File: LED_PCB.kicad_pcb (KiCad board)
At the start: 4 copper layers, 39.8 x 39.8 mm, 178 parts, among them J1 +5v Pad, J10 UART Debug, J11 UART Top (RX), J12 UART Bottom (TX), J13 UART Left (RX), J14 UART Right (TX), J15 ENA Pad, J16 MTX Out Conn, J2 +5v Pad, J3 +5v Pad, J4 +5v Pad, J5 GND Pad, J6 GND Pad, J7 GND Pad, J8 GND Pad, J9 ST-Link Conn, P1 USB_C_Plug_USB2.0, Q1 Si2319CDS, Q2 BSS138, SW1 SW_DP3T, SW2 SW_reset, SW3 SW_DPDT_x2, U1 AMS1117-3.3, U2 TPD4EUSB30, U3 STM32F103C8Tx, Y1 8MHz

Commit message: Inited repo
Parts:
- removed P1: USB_C_Plug_USB2.0, Connector_USB:USB_C_Receptacle_Amphenol_12401610E4-2A_CircularHoles
- added C76: 4.7u, Capacitor_Tantalum_SMD:CP_EIA-3216-12_Kemet-S, F.Cu at (79.4, 52.2)
- added J17: USB_C_Receptacle_USB2.0, LED_PCB_LIB:USB_C_Connector_16P_SMD, F.Cu at (74.5, 40.0)
- added R11: 1k5, Resistor_SMD:R_0402_1005Metric, F.Cu at (95.7, 35.0)
- added R12: 5.1k, Resistor_SMD:R_0402_1005Metric, F.Cu at (77.7, 41.8)
- added R13: 5.1k, Resistor_SMD:R_0402_1005Metric, F.Cu at (77.7, 38.8)
- C1: value 22u t -> 4.7u; footprint Capacitor_SMD:C_0504_1310Metric -> Capacitor_Tantalum_SMD:CP_EIA-3216-12_Kemet-S
- C12, C13, C14, C15, C16, C17, C18, C19, C20, C21, C22, C23, C24, C25, C26, C27, C28, C29, C30, C31, C32, C33, C34, C35, C36, C37, C38, C39, C40, C41, C42, C43, C44, C45, C46, C47, C48, C49, C50, C51, C52, C53, C54, C55, C56, C57, C58, C59, C60, C61, C62, C63, C64, C65, C66, C67, C68, C69, C70, C71, C72, C73, C74, C75: moved to F.Cu
- C2: footprint Capacitor_SMD:C_0504_1310Metric -> Capacitor_SMD:C_0805_2012Metric
- C5: value 4.7u -> 22u t
- moved C68 82.5 mm to (30.9, 30.8), turned to 0 degrees
- moved C52 77.0 mm to (33.4, 29.0), turned to 0 degrees
- moved C60 73.4 mm to (40.7, 27.2), turned to 0 degrees
- moved J16 72.6 mm to (124.1, 17.9), turned to 0 degrees
- moved C36 69.9 mm to (35.8, 34.2), turned to 0 degrees
- moved C70 68.5 mm to (35.8, 29.0), turned to 0 degrees
- moved C62 67.9 mm to (30.9, 39.5), turned to 0 degrees
- moved C53 67.2 mm to (38.2, 30.8), turned to 0 degrees
- moved J10 67.1 mm to (124.1, 21.2), turned to 0 degrees
- moved C69 66.8 mm to (40.7, 32.5), turned to 0 degrees
- moved C55 64.1 mm to (30.9, 32.5), turned to 0 degrees
- moved C13 63.6 mm to (35.8, 27.2), turned to 0 degrees
- moved C20 63.3 mm to (40.7, 37.8), turned to 0 degrees
- moved C38 63.0 mm to (33.4, 32.5), turned to 0 degrees
- moved C63 63.0 mm to (38.2, 27.2), turned to 0 degrees
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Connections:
- net /USB_DM renamed /USB_D-
- net /USB_DP renamed /USB_D+
- C5 pad 1: +3V3 -> +5V
- J9 pad 2: /SWCLK -> unconnected-(J9-Pad2)
- J9 pad 3: /SWDIO -> /SWCLK
- J9 pad 4: /NRST -> /SWDIO
- J9 pad 5: (no net) -> /NRST
- Q2 pad 2: /LED_MATRIX -> Net-(Q2-Pad2)
- R5 pad 1: /HSE_OUT -> Net-(C4-Pad1)
- R5 pad 2: Net-(C4-Pad1) -> /HSE_OUT
- R9 pad 1: /LED_MATRIX -> Net-(Q2-Pad2)
- U2 pad 5: (no net) -> unconnected-(U2-Pad5)
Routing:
- net +3V3: track 7.67 -> 47.2 mm, vias 0 -> 6
- net Net-(D51-Pad1): track 39.2 -> 5.56 mm
- net Net-(D59-Pad1): track 39.2 -> 5.56 mm
- net Net-(D19-Pad1): track 39.2 -> 5.56 mm
- net Net-(D27-Pad1): track 39.2 -> 5.61 mm
- net Net-(D11-Pad1): track 39.2 -> 5.67 mm
- net Net-(D35-Pad1): track 39.2 -> 6.67 mm, vias 0 -> 2
- net Net-(D43-Pad1): track 39.2 -> 8.11 mm, vias 0 -> 2
- net /UART2_TX: track 0.00 -> 26.7 mm, vias 0 -> 1
- net GND: track 7.81 -> 29.4 mm, vias 1 -> 21
- net /ENA_PIN: track 0.00 -> 17.2 mm
- net +5V: track 4.57 -> 20.3 mm, vias 1 -> 19
- net /BOOT0: track 0.00 -> 14.6 mm
- net /USB_D+: track 0.00 -> 14.5 mm
- net /USB_D-: track 0.00 -> 13.5 mm
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- added copper zone on F.Cu, net +3V3
- added copper zone on In1.Cu, net +3V3
- added copper zone on B.Cu, net +5V
- added copper zone on F.Cu, net +5V
- added copper zone on In2.Cu, net +5V
- added copper zone on B.Cu, net GND
- added copper zone on F.Cu, net GND
- added copper zone on In2.Cu, net GND
- added copper zone on B.Cu, net Net-(J1-Pad1)
- added copper zone on F.Cu, net Net-(J1-Pad1)
- added copper zone on In1.Cu, net Net-(J1-Pad1)
- removed copper zone on In1.Cu, net +5V
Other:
- board size 39.8 x 39.8 mm -> 40.3 x 39.8 mm

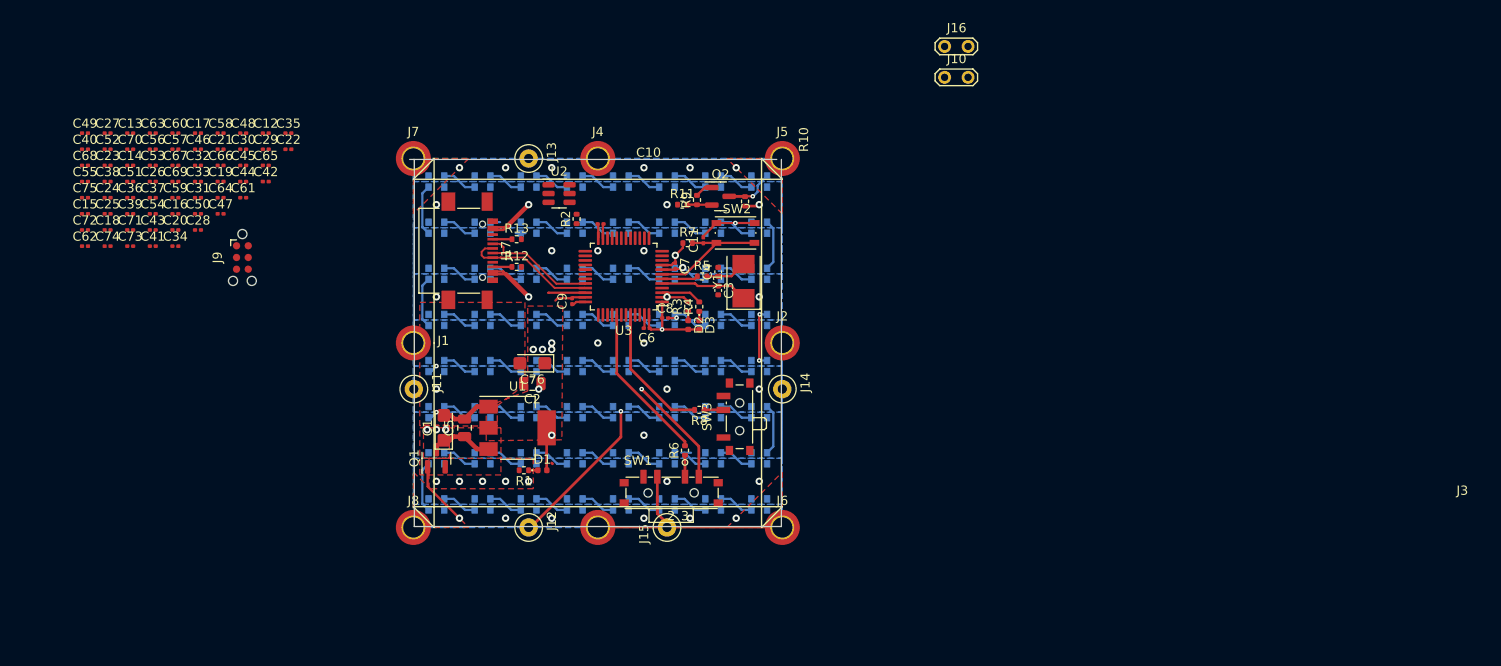
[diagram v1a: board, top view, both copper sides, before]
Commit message: traced power polygons
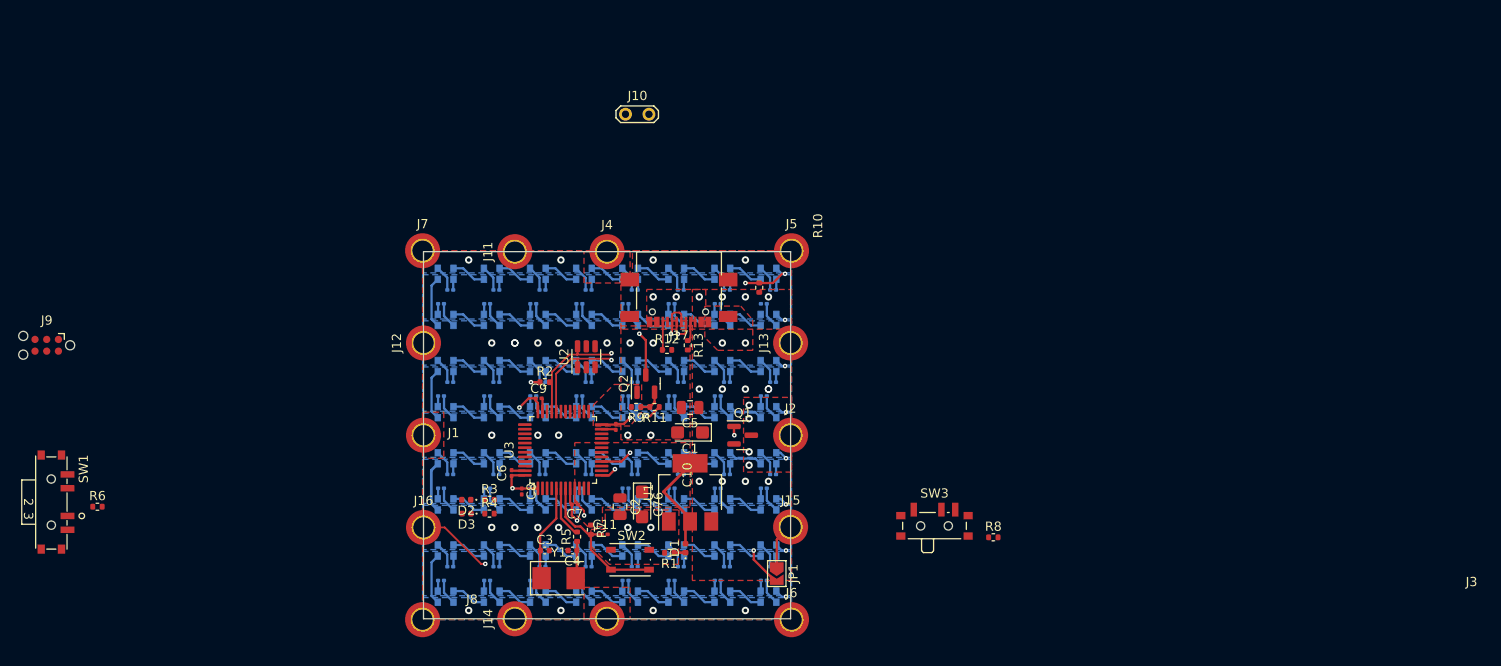
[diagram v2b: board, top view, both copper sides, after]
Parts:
- added JP1: Jumper_2_Open, Jumper:SolderJumper-2_P1.3mm_Open_TrianglePad1.0x1.5mm, F.Cu at (105.9, 75.0)
- C12, C13, C14, C15, C16, C17, C18, C19, C20, C21, C22, C23, C24, C25, C26, C27, C28, C29, C30, C31, C32, C33, C34, C35, C36, C37, C38, C39, C40, C41, C42, C43, C44, C45, C46, C47, C48, C49, C50, C51, C52, C53, C54, C55, C56, C57, C58, C59, C60, C61, C62, C63, C64, C65, C66, C67, C68, C69, C70, C71, C72, C73, C74, C75: moved to B.Cu
- J11, J12, J13, J14: footprint TestPoint:TestPoint_Loop_D1.80mm_Drill1.0mm_Beaded -> MountingHole:MountingHole_2.2mm_M2_DIN965_Pad_TopOnly
- J15: value ENA Pad -> LED_MATRIX_IN; footprint TestPoint:TestPoint_Loop_D1.80mm_Drill1.0mm_Beaded -> MountingHole:MountingHole_2.2mm_M2_DIN965_Pad_TopOnly
- J16: value MTX Out Conn -> Matrix_pad; footprint TestPoint:TestPoint_2Pads_Pitch2.54mm_Drill0.8mm -> MountingHole:MountingHole_2.2mm_M2_DIN965_Pad_TopOnly
- moved J16 76.9 mm to (67.6, 70.0)
- moved C48 74.2 mm to (105.5, 74.2), turned to 180 degrees
- moved C52 73.7 mm to (105.5, 44.2), turned to 180 degrees
- moved C30 73.3 mm to (104.5, 75.8)
- moved C23 72.7 mm to (104.5, 45.8)
- moved C54 69.7 mm to (105.5, 54.2), turned to 180 degrees
- moved C37 69.7 mm to (104.5, 55.8)
- moved C31 69.2 mm to (105.5, 64.2), turned to 180 degrees
- moved C50 68.2 mm to (104.5, 65.8)
- moved C38 68.2 mm to (100.5, 44.2), turned to 180 degrees
- moved C43 67.7 mm to (100.5, 64.2), turned to 180 degrees
- moved C29 67.4 mm to (100.5, 74.2), turned to 180 degrees
- moved SW1 67.2 mm to (27.2, 67.2), turned to -90 degrees
- moved C24 67.1 mm to (99.5, 45.8)
- moved C53 66.5 mm to (100.5, 54.2), turned to 180 degrees
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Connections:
- J16 pad 1: GND -> Net-(D67-Pad1)
- SW1 pad 2: Net-(J15-Pad1) -> unconnected-(SW1-Pad2)
- U3 pad 12: unconnected-(U3-Pad12) -> /UART2_TX
- U3 pad 13: /UART2_TX -> /UART2_RX
- U3 pad 14: /UART2_RX -> unconnected-(U3-Pad14)
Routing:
- net GND: track 29.4 -> 187.1 mm, vias 21 -> 32
- net +5V: track 20.3 -> 73.2 mm, vias 19 -> 15
- net Net-(D67-Pad1): track 0.00 -> 43.6 mm, vias 0 -> 2
- net /LED_MATRIX: track 0.00 -> 33.7 mm, vias 0 -> 3
- net /UART2_TX: track 26.7 -> 0.00 mm, vias 1 -> 0
- net +3V3: track 47.2 -> 28.6 mm, vias 6 -> 5
- net Net-(D4-Pad3): track 6.66 -> 24.5 mm, vias 1 -> 3
- net /ENA_PIN: track 17.2 -> 0.00 mm
- net /BOOT0: track 14.6 -> 0.00 mm
- net /USB_D-: track 13.5 -> 24.1 mm, vias 0 -> 2
- net /USB_D+: track 14.5 -> 25.0 mm, vias 0 -> 2
- net /HSE_OUT: track 0.00 -> 5.60 mm
- net Net-(C4-Pad1): track 8.48 -> 4.05 mm
- net /SWDIO: track 4.01 -> 0.00 mm
- net Net-(D32-Pad1): track 0.00 -> 3.80 mm
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- removed copper zone on In2.Cu, net +5V
- removed copper zone on B.Cu, net Net-(J1-Pad1)
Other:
- board size 40.3 x 39.8 mm -> 39.8 x 39.8 mm

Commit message: traced rawly
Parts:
- added C77: 100n, Capacitor_SMD:C_0201_0603Metric, F.Cu at (86.0, 44.5)
- added J18: ENA_pad, TestPoint:TestPoint_Keystone_5000-5004_Miniature, F.Cu at (67.5, 55.0)
- added R14: 10k, Resistor_SMD:R_0402_1005Metric, F.Cu at (79.8, 47.2)
- added SW4: SW_reset, Button_Switch_SMD:SW_Push_1P1T_NO_Vertical_Wuerth_434133025816, F.Cu at (82.5, 44.8)
- J9: value ST-Link Conn -> ST-Link Tagcon
- JP1: value Jumper_2_Open -> EXT_SIGNAL
- moved J10 55.7 mm to (99.5, 80.0), turned to 180 degrees
- moved R8 53.7 mm to (76.5, 61.8)
- moved SW3 51.0 mm to (72.2, 64.6), turned to -90 degrees
- moved J9 48.0 mm to (74.5, 44.9)
- moved SW1 47.6 mm to (73.0, 54.1)
- moved R6 45.1 mm to (76.6, 59.7), turned to -90 degrees
- moved R10 8.10 mm to (101.8, 51.8), turned to 90 degrees
- moved JP1 6.17 mm to (103.6, 69.3), turned to 90 degrees
- moved D2 4.53 mm to (76.8, 67.0)
- moved D3 4.51 mm to (76.8, 68.2)
- moved R4 4.05 mm to (78.8, 68.2)
- moved R3 4.05 mm to (78.8, 67.0)
- moved C8 3.57 mm to (75.8, 63.5), turned to 90 degrees
- moved Q2 1.17 mm to (90.6, 54.0)
- moved C9 0.75 mm to (80.2, 55.2)
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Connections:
- D4 pad 3: Net-(D4-Pad3) -> /LED_MATRIX_5V
- J10 pad 1: /UART3_RX -> /UART2_RX
- J10 pad 2: /UART3_TX -> /UART2_TX
- J12 pad 1: /UART2_TX -> /UART3_TX
- J13 pad 1: /UART2_RX -> /UART3_RX
- J9 pad 1: GND -> +3V3
- J9 pad 2: unconnected-(J9-Pad2) -> /SWDIO
- J9 pad 3: /SWCLK -> /NRST
- J9 pad 4: /SWDIO -> /SWCLK
- J9 pad 5: /NRST -> GND
- J9 pad 6: (no net) -> unconnected-(J9-Pad6)
- JP1 pad 2: /LED_MATRIX -> /LED_MATRIX_5V
- Q2 pad 3: Net-(D4-Pad3) -> /LED_MATRIX_5V
- R10 pad 1: Net-(D4-Pad3) -> /LED_MATRIX_5V
- SW1 pad 2: unconnected-(SW1-Pad2) -> +3V3
- SW1 pad 4: +3V3 -> Net-(J18-Pad1)
- U3 pad 28: unconnected-(U3-Pad28) -> /USR_BTN
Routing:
- net /LED_MATRIX_5V: track 0.00 -> 46.2 mm, vias 0 -> 5
- net /NRST: track 16.5 -> 51.9 mm, vias 0 -> 2
- net /UART1_TX: track 0.00 -> 31.0 mm, vias 0 -> 2
- net /UART3_TX: track 0.00 -> 28.3 mm, vias 0 -> 2
- net /UART3_RX: track 0.00 -> 27.3 mm, vias 0 -> 2
- net Net-(D4-Pad3): track 24.5 -> 0.00 mm, vias 3 -> 0
- net /UART2_TX: track 0.00 -> 24.2 mm, vias 0 -> 1
- net /SWDIO: track 0.00 -> 22.7 mm, vias 0 -> 2
- net /LED_MATRIX: track 33.7 -> 11.0 mm, vias 3 -> 2
- net /UART2_RX: track 1.74 -> 23.0 mm
- net /UART1_RX: track 0.00 -> 20.3 mm, vias 0 -> 2
- net /USR_BTN: track 0.00 -> 19.9 mm, vias 0 -> 2
- net /SWCLK: track 0.00 -> 18.6 mm, vias 0 -> 2
- net +3V3: track 28.6 -> 43.1 mm, vias 5 -> 14
- net Net-(J18-Pad1): track 0.00 -> 7.89 mm
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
